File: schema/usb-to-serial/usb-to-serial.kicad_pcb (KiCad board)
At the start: 2 copper layers, 29 x 57 mm, 36 parts, among them P1 CONN_6X2, Q1 MOS_P, U1 FT232BL, U2 LP5951MF-3.3, U3 MINI-USB-B, X1 CRYSTAL

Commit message: t
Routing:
- net GND: track 30.2 -> 62.3 mm
- removed copper zone on F.Cu, net GND
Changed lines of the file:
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@@
   (general
     (links 80)
-    (no_connects 49)
+    (no_connects 45)
     (area 181.11055 100.06006 211.075001 159.075001)
     (thickness 1.6)
     (drawings 4)
-    (tracks 111)
+    (tracks 124)
     (zones 0)
     (modules 36)
@@
   (segment (start 200.2 130) (end 200.2 133.2) (width 0.4) (layer F.Cu) (net 14))
   (segment (start 199.77368 129.57368) (end 200.2 130) (width 0.4) (layer F.Cu) (net 14))
+  (segment (start 192.6 108.2) (end 192.4 108.4) (width 0.4) (layer F.Cu) (net 20))
+  (segment (start 192.6 108.2) (end 196 108.2) (width 0.4) (layer F.Cu) (net 20))
+  (segment (start 196 108.2) (end 196.4 108.6) (width 0.4) (layer F.Cu) (net 20))
+  (segment (start 196.4 108.6) (end 196.4 110) (width 0.4) (layer F.Cu) (net 20))
+  (segment (start 196.4 110) (end 196.45172 109.94828) (width 0.4) (layer F.Cu) (net 20))
+  (segment (start 198.49834 109.94828) (end 196.45172 109.94828) (width 0.4) (layer F.Cu) (net 20) (status 400000))
+  (segment (start 192.4 109.94594) (end 192.40234 109.94828) (width 0.4) (layer F.Cu) (net 20) (status C00000))
+  (segment (start 192.4 108.4) (end 192.4 109.94594) (width 0.4) (layer F.Cu) (net 20) (status 800000))
+  (segment (start 198.49834 104.45172) (end 198.49834 109.94828) (width 0.4) (layer F.Cu) (net 20) (status C00000))
+  (segment (start 189.50166 104.45172) (end 198.49834 104.45172) (width 0.4) (layer F.Cu) (net 20) (status C00000))
+  (segment (start 189.60072 109.94828) (end 189.60072 104.55078) (width 0.4) (layer F.Cu) (net 20) (status C00000))
+  (segment (start 189.60072 104.55078) (end 189.50166 104.45172) (width 0.4) (layer F.Cu) (net 20) (status C00000))
+  (segment (start 192.40234 109.94828) (end 189.60072 109.94828) (width 0.4) (layer F.Cu) (net 20) (status C00000))
   (segment (start 194.1 124.9) (end 194.1 125.9) (width 0.4) (layer F.Cu) (net 20))
   (segment (start 191.206 129.794) (end 191.206 131.5498) (width 0.4) (layer F.Cu) (net 20))
@@
   (segment (start 195 120.2) (end 195.2 120.4) (width 0.4) (layer F.Cu) (net 38))
   (segment (start 194.42418 120.77582) (end 195 120.2) (width 0.4) (layer F.Cu) (net 38))
-  (zone (net 20) (net_name GND) (layer F.Cu) (hatch edge 0.508)
-    (connect_pads (clearance 1))
-    (min_thickness 0.5)
-    (fill (arc_segments 16) (thermal_gap 5.08) (thermal_bridge_width 5.08))
-    (polygon
-      (pts
-        (xy 199.8 111.8) (xy 196.4 111.8) (xy 196.4 108.4) (xy 191.6 108.4) (xy 191.6 111.8)
-        (xy 188.2 111.8) (xy 188.2 111.6) (xy 188.2 102) (xy 199.8 102)
-      )
-    )
-  )
 )

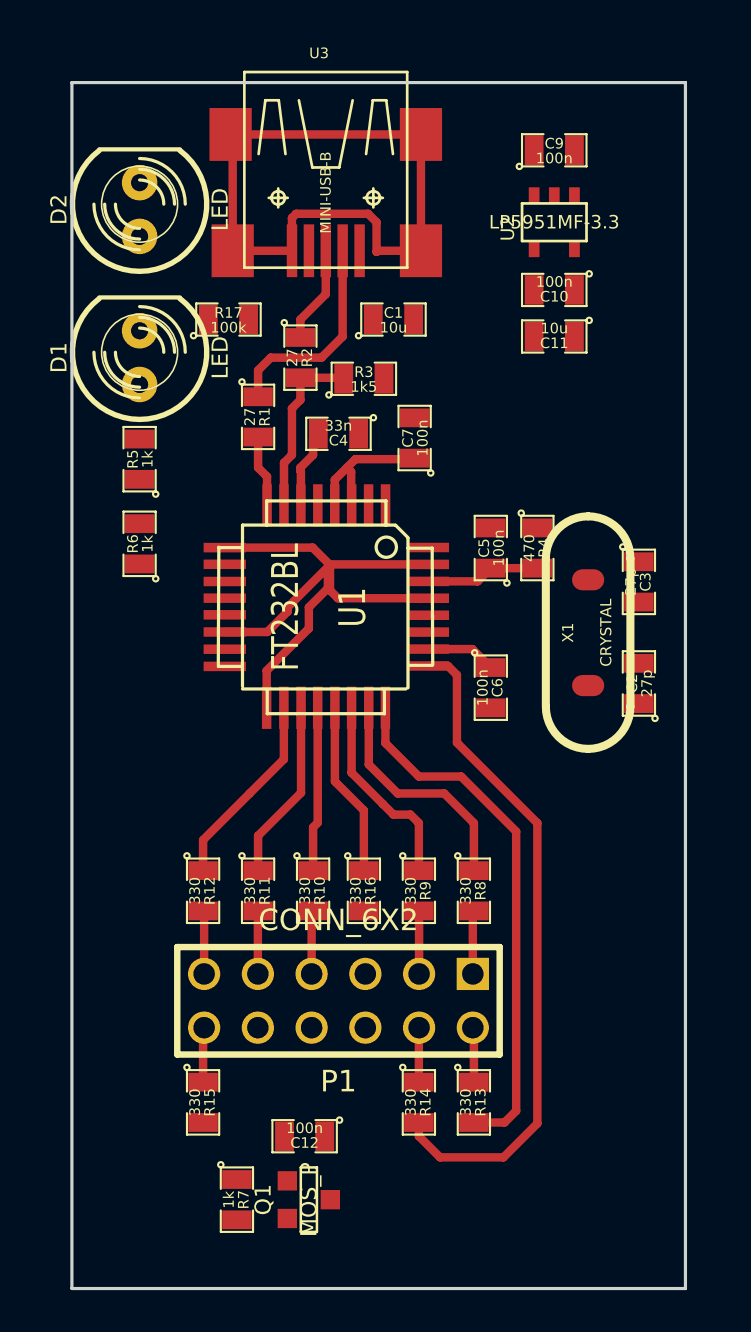
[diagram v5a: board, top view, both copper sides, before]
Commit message: Zones doesn't work in the new KiCad version 2013-03-19.
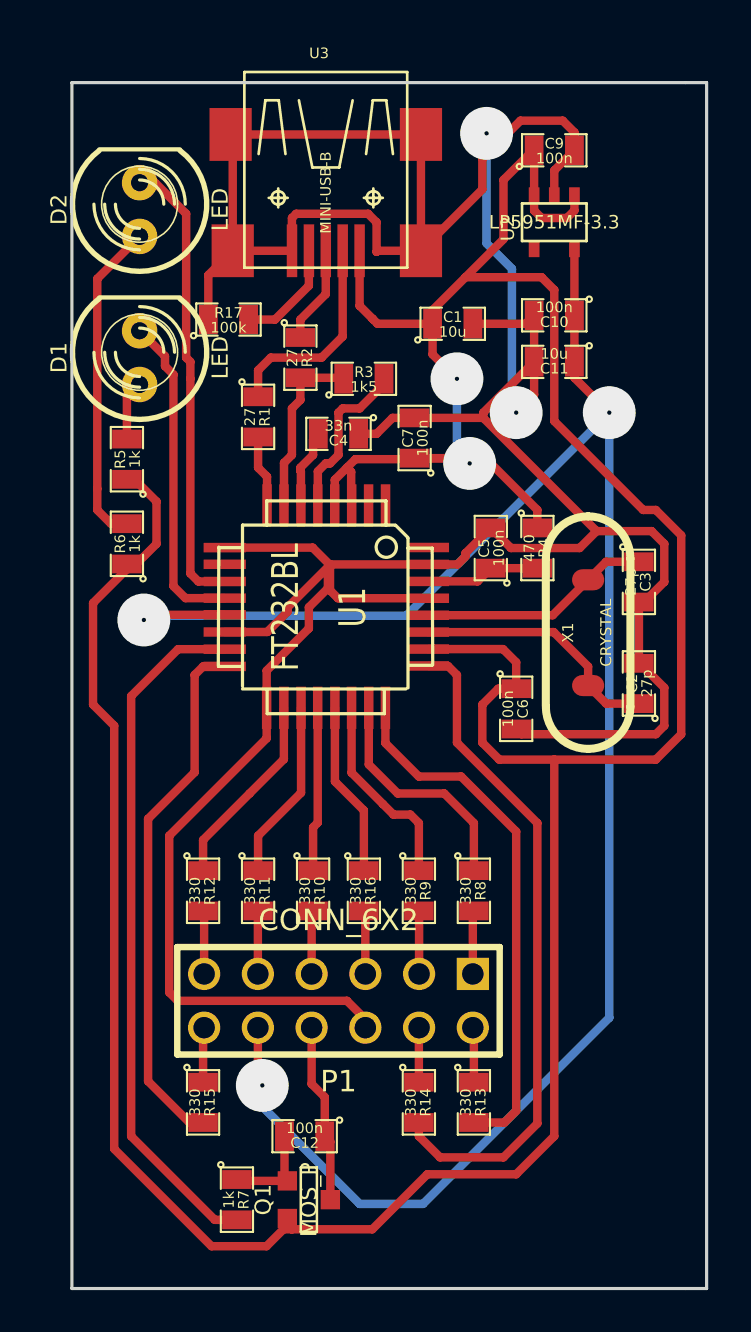
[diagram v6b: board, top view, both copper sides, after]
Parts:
- moved C1 2.81 mm to (200.0, 113.4)
- moved C6 1.56 mm to (203.0, 131.6)
- moved C10 1.20 mm to (204.8, 113.0)
- moved C11 1.20 mm to (204.8, 115.2)
- moved R5 0.60 mm to (184.6, 119.8)
- moved R6 0.60 mm to (184.6, 123.8)
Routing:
- net VCC: track 10.6 -> 172.9 mm, vias 0 -> 2
- net GND: track 62.3 -> 175.8 mm, vias 0 -> 2
- net +3.3V: track 0.00 -> 92.8 mm, vias 0 -> 3
- net /pwren: track 0.00 -> 32.8 mm
- net /txden: track 0.00 -> 25.1 mm
- net /rxled: track 0.00 -> 21.7 mm
- net N-0000037: track 0.00 -> 15.4 mm
- net /txled: track 0.00 -> 15.4 mm
- net /xtal1: track 0.00 -> 11.9 mm
- net /xtal2: track 0.00 -> 11.0 mm
- net /vccout: track 0.00 -> 8.50 mm
- net /rstout: track 0.00 -> 7.87 mm
- net N-0000025: track 0.00 -> 5.16 mm
- net N-0000027: track 0.00 -> 4.58 mm
- net N-0000023: track 0.00 -> 3.01 mm
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- added copper zone on F.Cu, net GND
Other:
- board size 29 x 57 mm -> 30 x 57 mm
